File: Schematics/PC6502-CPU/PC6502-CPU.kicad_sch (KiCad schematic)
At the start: 71 parts, among them J1 BUS, J2 CONSOLE, J4 TEST, J5 Conn_02x05_Odd_Even, J6 Conn_02x02_Odd_Even, U1 MC68B50, U2 628128_DIP32_SSOP32, U3 SST39SF010, U4 ATF1502AS, U5 W65C02, U6 74AHC244, U7 74LS161, X1 CXO_DIP8, X2 ASCO

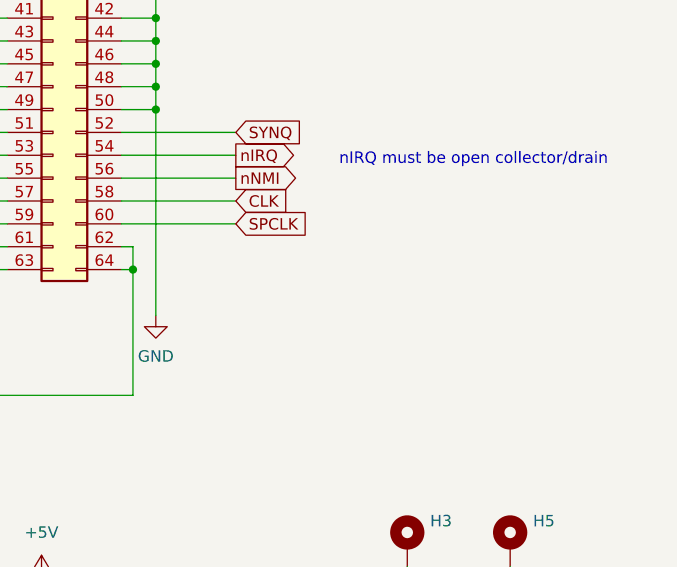
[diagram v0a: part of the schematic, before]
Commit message: Add Power/Storage PCB
Also tidied template
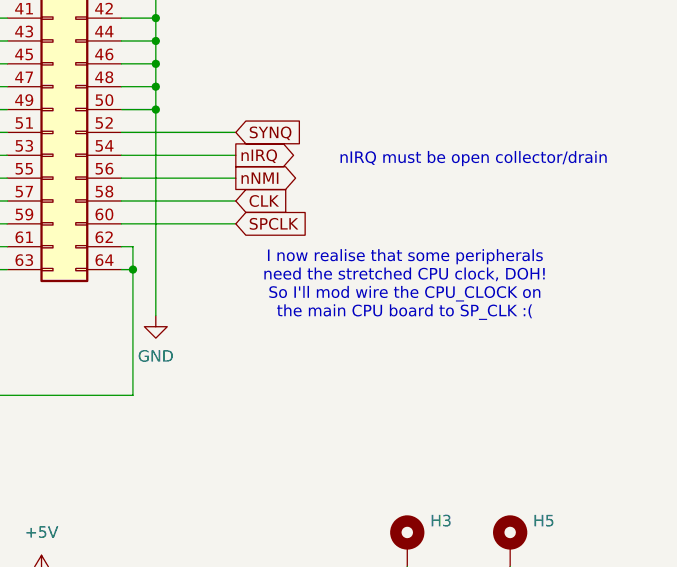
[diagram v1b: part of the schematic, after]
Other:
- note added: "I now realise that some peripherals need the stretched CPU clock, DOH! So I'll mod wire the CPU_CLOCK on the main CPU board to SP_CLK :("
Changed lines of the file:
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@@
+		)
+	)
+	(text "I now realise that some peripherals \nneed the stretched CPU clock, DOH!\nSo I'll mod wire the CPU_CLOCK on \nthe main CPU board to SP_CLK :("
+		(exclude_from_sim no)
+		(at 385.826 194.818 0)
+		(effects
+			(font
+				(size 1.27 1.27)
+			)
 		)
 	)

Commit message: Created V1.1 Schematic and PCB
A LOT of changes from v1.00;
removed clock stretcher (will now live in the CPLD)
moved the USB interface direct to the PCB
changed power pins
Added extra capacitance
Used Grant Searle's OSI basic and memory map to bring up the board
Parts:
- removed C10, C7: 100nF, Capacitor_SMD:C_0805_2012Metric, symbol Device:C
- removed D9: 1N4148, Diode_THT:D_DO-35_SOD27_P7.62mm_Horizontal, symbol Diode:1N4148
- removed J2: CONSOLE, Connector_PinHeader_2.54mm:PinHeader_1x03_P2.54mm_Horizontal, symbol Connector_Generic:Conn_01x03
- removed R17, R18: 0R, Resistor_SMD:R_0603_1608Metric_Pad0.98x0.95mm_HandSolder, symbol Device:R
- removed TP2, TP3, TP4: TestPoint, TestPoint:TestPoint_Loop_D1.80mm_Drill1.0mm_Beaded, symbol Connector:TestPoint
- removed U1: MC68B50, Package_DIP:DIP-24_W15.24mm_Socket, symbol Interface_UART:MC68B50
- removed U2: 628128_DIP32_SSOP32, Package_DIP:DIP-32_W15.24mm_LongPads, symbol Memory_RAM:628128_DIP32_SSOP32
- removed U7: 74LS161, Package_DIP:DIP-16_W7.62mm_Socket, symbol 74xx:74LS161
- removed X2: ASCO, Oscillator:Oscillator_SMD_EuroQuartz_XO91-4Pin_7.0x5.0mm_HandSoldering, symbol Oscillator:ASCO
- added C7: 47uF, Capacitor_SMD:C_1206_3216Metric, symbol Device:C_Polarized_US
- added U2: AS6C4008-55PCN, Package_DIP:DIP-32_W15.24mm, symbol Memory_RAM:AS6C4008-55PCN
- added U8: MCP130-450DI/TO, Package_TO_SOT_THT:TO-92_Inline, symbol Power_Supervisor:MCP130-xxxDxTO
- R15, R23, R24: value 4K7 -> 10K
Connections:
- net PHI2x2 is gone; now on net SYSCLK: X1.5 (OUT)
- net SPCLK is gone; now on net CPU_CLK: J1.60 (Pin_60)
- net +5V: now also C11.2, J1.12 (Pin_12), J1.16 (Pin_16), J1.20 (Pin_20), J1.24 (Pin_24), J1.28 (Pin_28), J1.32 (Pin_32), J1.36 (Pin_36), J1.4 (Pin_4), J1.40 (Pin_40), J1.44 (Pin_44), J1.48 (Pin_48), J1.8 (Pin_8), R6.2, R7.2, C7.1, U2.32 (VCC), U8.2 (VDD); no longer J1.59 (Pin_59), J1.61 (Pin_61), J1.62 (Pin_62), J1.63 (Pin_63), J1.64 (Pin_64), R15.1, R24.1
- net A0: now also U2.12 (A0)
- net A1: now also U2.11 (A1); no longer U4.11 (I/O/PD1)
- net A10: now also U2.23 (A10)
- net A11: now also U2.25 (A11)
- net A12: now also U2.4 (A12)
- net A13: now also U2.28 (A13)
- net A14: now also U2.3 (A14); no longer U3.29 (A14)
- net A2: now also U2.10 (A2); no longer U4.6 (I/O)
- net A3: now also U2.9 (A3); no longer U4.8 (I/O)
- net A4: now also U2.8 (A4)
- net A5: now also U2.7 (A5)
- net A6: now also U2.6 (A6)
- net A7: now also U2.5 (A7)
- net A8: now also U2.27 (A8)
- net A9: now also U2.26 (A9)
- net D0: now also U2.13 (DQ0)
- net D1: now also U2.14 (DQ1)
- net D2: now also U2.15 (DQ2)
- net D3: now also U2.17 (DQ3)
- net D4: now also U2.18 (DQ4)
- net D5: now also U2.19 (DQ5)
- net D6: now also U2.20 (DQ6)
- net D7: now also U2.21 (DQ7)
- net GND: now also C11.1, J1.64 (Pin_64), R15.2, R24.2, C7.2, U2.16 (VSS), U8.3 (VSS); no longer C11.2, J1.12 (Pin_12), J1.16 (Pin_16), J1.20 (Pin_20), J1.24 (Pin_24), J1.28 (Pin_28), J1.32 (Pin_32), J1.36 (Pin_36), J1.4 (Pin_4), J1.40 (Pin_40), J1.44 (Pin_44), J1.48 (Pin_48), J1.8 (Pin_8), R6.2, R7.2
- net RAM_A15: now also U2.31 (A15); no longer J4.2 (Pin_2), U6.13 (2A2)
- net RAM_A16: now also U2.2 (A16); no longer U6.11 (2A3)
- net nBUSRQ: now also J1.61 (Pin_61); no longer J1.55 (Pin_55)
- net nIRQ: now also U6.11 (2A3)
- net nR: now also U2.24 (OE#)
- net nRAM_CS: now also U2.22 (CE#)
- net nRES: now also J1.63 (Pin_63), J4.6 (Pin_6), RN1.4 (R3), U4.8 (I/O), U6.6 (1A2), U8.1 (~{RST}); no longer C11.1, J1.57 (Pin_57), R15.2
- net nW: now also U2.29 (WE#)
- net RDY: now reaches R19.2, U5.2 (RDY)
- net RDY: now also J1.57 (Pin_57)
- net at R23.2: now also U2.30 (A17)
- net nVP: now reaches U5.1 (VPB)
- net nVP: now also J1.59 (Pin_59)
- net at D8.1 (K): now also U6.9 (2Y3); no longer R7.1
- net at D8.2 (A): now also R7.1; no longer U6.9 (2Y3)
- net nRXF: now reaches U4.1 (I/GCLR)
- net nWR_FT: now reaches U4.41 (I/O/GCLK3)
- net nTXE: now reaches U4.44 (I/OE1)
- net at R6.1: now also D7.2 (A); no longer D7.1 (K)
- net at U6.7 (2Y2): now also D7.1 (K); no longer D7.2 (A)
- net 6850_E renamed nRD_FT
- net CLK renamed SYSCLK
- net ROM_A16 renamed ROM_A14
- net ROM_A14: now also U3.29 (A14); no longer U3.2 (A16)
- removed net nCONSOLE_CS: J4.6 (Pin_6), RN1.4 (R3), U4.29 (I/O), U6.6 (1A2)
- net nSLOW renamed nSLOW0
- net nSLOW0: now also U4.11 (I/O/PD1)
- new net: R15.1, U3.2 (A16)
- new net: R24.1, U2.1 (A18)
- new net RAM_A17: U4.29 (I/O)
- new net nSLOW1: J1.55 (Pin_55), J4.2 (Pin_2), U4.6 (I/O), U6.13 (2A2)
- no-connect marks 13 -> 8
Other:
- added sheet 60FAKE50 (60FAKE50.kicad_sch)
- note added: "CPU_CLK is the stretched version of CLK. Use nSLOW0 and nSLOW1 to slow the clock down"
- note added: "FLAGs are passed to the CPLD The CPLD "pretends" to be the 6850 register for status"
- note added: "For AS6C1008 remove R24"
- note added: "IRQ"
- note added: "MCP130 has internal 5K1 Pull up on ~{RST}"
- note added: "RESET"
- note added: "SLOW0"
- note added: "SLOW1"
- note removed: "CONSOLE"
- note removed: "I now realise that some peripherals need the stretched CPU clock, DOH! So I'll mod wire the CPU_CLOCK on the main CPU board to SP_CLK :("
- note removed: "If ROM isn't working, take OE to RnW direct"
- note removed: "RAMA15"
- note removed: "RAMA16"
- note removed: "SLOW"
- moved on the sheet: D7, D8, J5, R10, R13, R14, R16, S1

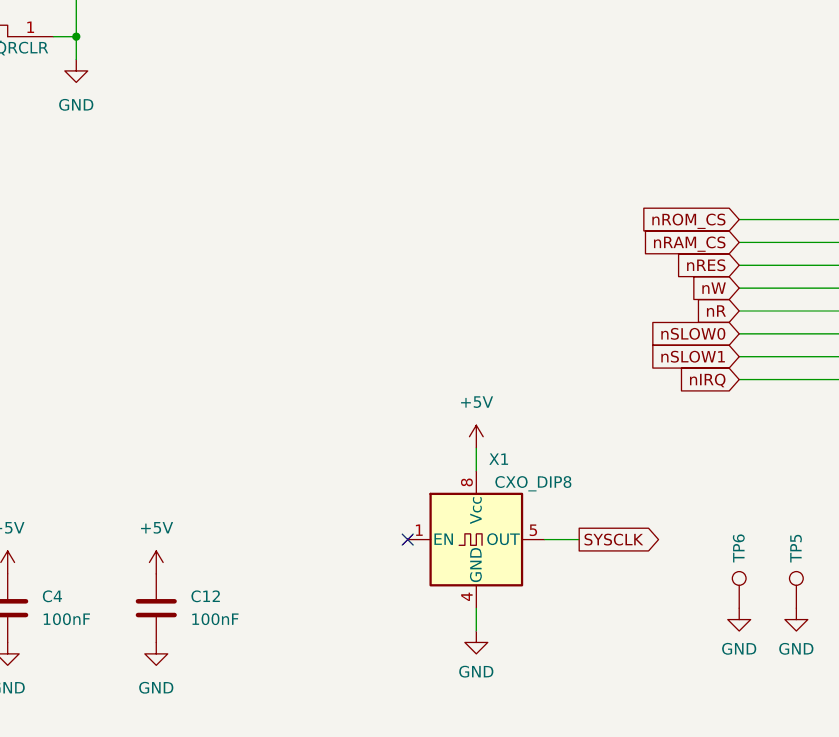
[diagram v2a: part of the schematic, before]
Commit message: FT245 WRITE signal correction
I had it marked as active low when it's active high, updated.
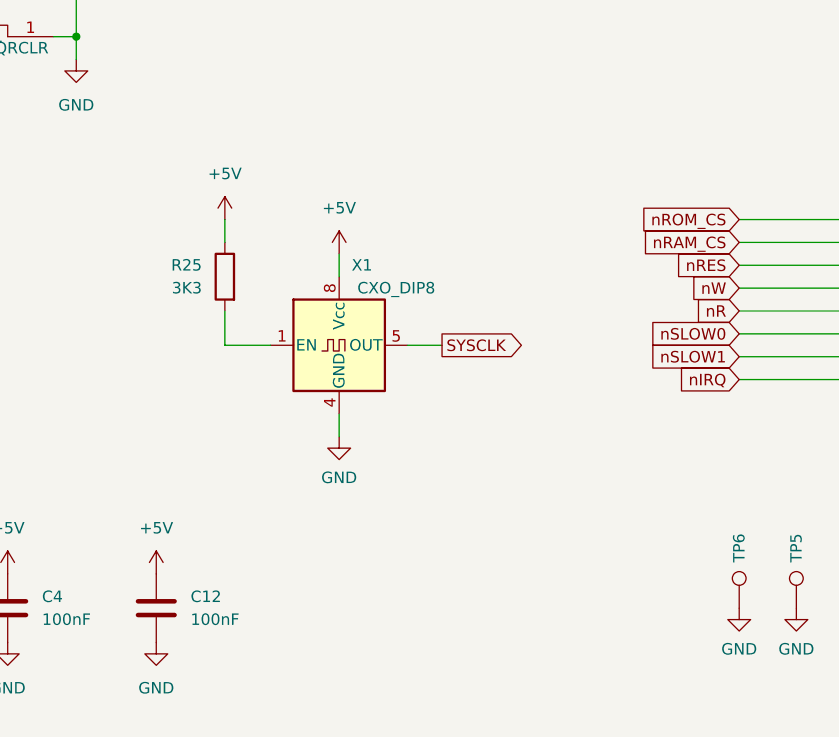
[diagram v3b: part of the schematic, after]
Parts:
- added R25: 3K3, Resistor_SMD:R_0603_1608Metric_Pad0.98x0.95mm_HandSolder, symbol Device:R
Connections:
- net +5V: now also R25.1
- net at X1.1 (EN): now also R25.2
- no-connect marks 8 -> 7
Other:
- moved on the sheet: X1
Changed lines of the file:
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@@
 	)
 	(no_connect
-		(at 124.46 257.81)
-	)
-	(no_connect
 		(at 64.77 149.86)
 	)
@@
 	(wire
 		(pts
+			(xy 104.14 236.22) (xy 104.14 232.41)
+		)
+		(stroke
+			(width 0)
+			(type default)
+		)
+	)
+	(wire
+		(pts
 			(xy 161.29 82.55) (xy 161.29 90.17)
 		)
@@
 	(wire
 		(pts
-			(xy 139.7 257.81) (xy 143.51 257.81)
+			(xy 124.46 236.22) (xy 128.27 236.22)
 		)
 		(stroke
@@
 	(wire
 		(pts
-			(xy 132.08 247.65) (xy 132.08 250.19)
+			(xy 116.84 226.06) (xy 116.84 228.6)
 		)
 		(stroke
@@
 		)
 	)
+	(wire
+		(pts
+			(xy 109.22 236.22) (xy 104.14 236.22)
+		)
+		(stroke
+			(width 0)
+			(type default)
+		)
+	)
 	(bus
 		(pts
@@
 	(wire
 		(pts
-			(xy 132.08 265.43) (xy 132.08 267.97)
+			(xy 116.84 243.84) (xy 116.84 246.38)
 		)
 		(stroke
@@
 	(wire
 		(pts
+			(xy 104.14 222.25) (xy 104.14 224.79)
+		)
+		(stroke
+			(width 0)
+			(type default)
+		)
+	)
+	(wire
+		(pts
 			(xy 86.36 43.18) (xy 71.12 43.18)
 		)
@@
 	(global_label "SYSCLK"
 		(shape output)
-		(at 143.51 257.81 0)
+		(at 128.27 236.22 0)
 		(fields_autoplaced yes)
 		(effects
@@
 		)
 		(property "Intersheetrefs" "${INTERSHEET_REFS}"
-			(at 153.5709 257.81 0)
+			(at 138.3309 236.22 0)
 			(effects
 				(font
@@
 	(symbol
 		(lib_id "power:+5V")
-		(at 132.08 247.65 0)
+		(at 116.84 226.06 0)
 		(unit 1)
 		(exclude_from_sim no)
@@
 		(fields_autoplaced yes)
 		(property "Reference" "#PWR033"
-			(at 132.08 251.46 0)
+			(at 116.84 229.87 0)
 			(effects
 				(font
@@
 		)
 		(property "Value" "+5V"
-			(at 132.08 242.57 0)
+			(at 116.84 220.98 0)
 			(effects
 				(font
@@
 		)
 		(property "Footprint" ""
-			(at 132.08 247.65 0)
+			(at 116.84 226.06 0)
 			(effects
 				(font
@@
 		)
 		(property "Datasheet" ""
-			(at 132.08 247.65 0)
+			(at 116.84 226.06 0)
 			(effects
 				(font
@@
 		)
 		(property "Description" ""
-			(at 132.08 247.65 0)
+			(at 116.84 226.06 0)
 			(effects
 				(font
@@
 	(symbol
 		(lib_id "power:GND")
-		(at 132.08 267.97 0)
+		(at 116.84 246.38 0)
 		(unit 1)
 		(exclude_from_sim no)
@@
 		(fields_autoplaced yes)
 		(property "Reference" "#PWR07"
-			(at 132.08 274.32 0)
+			(at 116.84 252.73 0)
 			(effects
 				(font
@@
 		)
 		(property "Value" "GND"
-			(at 132.08 272.5325 0)
+			(at 116.84 250.9425 0)
 			(effects
 				(font
@@
 		)
 		(property "Footprint" ""
-			(at 132.08 267.97 0)
+			(at 116.84 246.38 0)
 			(effects
 				(font
@@
 		)
 		(property "Datasheet" ""
-			(at 132.08 267.97 0)
+			(at 116.84 246.38 0)
 			(effects
 				(font
@@
 		)
 		(property "Description" ""
-			(at 132.08 267.97 0)
+			(at 116.84 246.38 0)
 			(effects
 				(font
@@
 	)
 	(symbol
+		(lib_id "Device:R")
+		(at 104.14 228.6 0)
+		(mirror y)
+		(unit 1)
+		(exclude_from_sim no)
+		(in_bom yes)
+		(on_board yes)
+		(dnp no)
+		(fields_autoplaced yes)
+		(property "Reference" "R25"
+			(at 101.6 227.3299 0)
+			(effects
+				(font
+					(size 1.27 1.27)
+				)
+				(justify left)
+			)
+		)
+		(property "Value" "3K3"
+			(at 101.6 229.8699 0)
+			(effects
+				(font
+					(size 1.27 1.27)
+				)
+				(justify left)
+			)
+		)
+		(property "Footprint" "Resistor_SMD:R_0603_1608Metric_Pad0.98x0.95mm_HandSolder"
+			(at 105.918 228.6 90)
+			(effects
+				(font
+					(size 1.27 1.27)
+				)
+				(hide yes)
+			)
+		)
+		(property "Datasheet" "~"
+			(at 104.14 228.6 0)
+			(effects
+				(font
+					(size 1.27 1.27)
+				)
+				(hide yes)
+			)
+		)
+		(property "Description" ""
+			(at 104.14 228.6 0)
+			(effects
+				(font
+					(size 1.27 1.27)
+				)
+			)
+		)
+		(pin "1"
+		)
+		(pin "2"
+		)
+		(instances
+			(project "PC6502-CPU"
+				(path "/f3365b77-bdc1-4fa0-8030-841dab6ab2be"
+					(reference "R25")
+					(unit 1)
+				)
+			)
+		)
+	)
+	(symbol
 		(lib_id "power:+5V")
 		(at 134.62 66.04 0)
@@
 	)
 	(symbol
+		(lib_id "power:+5V")
+		(at 104.14 222.25 0)
+		(mirror y)
+		(unit 1)
+		(exclude_from_sim no)
+		(in_bom yes)
+		(on_board yes)
+		(dnp no)
+		(fields_autoplaced yes)
+		(property "Reference" "#PWR050"
+			(at 104.14 226.06 0)
+			(effects
+				(font
+					(size 1.27 1.27)
+				)
+				(hide yes)
+			)
+		)
+		(property "Value" "+5V"
+			(at 104.14 217.17 0)
+			(effects
+				(font
+					(size 1.27 1.27)
+				)
+			)
+		)
+		(property "Footprint" ""
+			(at 104.14 222.25 0)
+			(effects
+				(font
+					(size 1.27 1.27)
+				)
+				(hide yes)
+			)
+		)
+		(property "Datasheet" ""
+			(at 104.14 222.25 0)
+			(effects
+				(font
+					(size 1.27 1.27)
+				)
+				(hide yes)
+			)
+		)
+		(property "Description" ""
+			(at 104.14 222.25 0)
+			(effects
+				(font
+					(size 1.27 1.27)
+				)
+			)
+		)
+		(pin "1"
+		)
+		(instances
+			(project "PC6502-CPU"
+				(path "/f3365b77-bdc1-4fa0-8030-841dab6ab2be"
+					(reference "#PWR050")
+					(unit 1)
+				)
+			)
+		)
+	)
+	(symbol
 		(lib_id "Device:LED")
 		(at 250.19 222.25 0)
@@
 	(symbol
 		(lib_id "Oscillator:CXO_DIP8")
-		(at 132.08 257.81 0)
+		(at 116.84 236.22 0)
 		(unit 1)
 		(exclude_from_sim no)
@@
 		(dnp no)
 		(property "Reference" "X1"
-			(at 134.62 248.92 0)
+			(at 119.38 227.33 0)
 			(effects
 				(font
@@
 		)
 		(property "Value" "CXO_DIP8"
-			(at 138.43 251.46 0)
+			(at 123.19 229.87 0)
 			(effects
 				(font
@@
 		)
 		(property "Footprint" "Oscillator:Oscillator_DIP-8"
-			(at 143.51 266.7 0)
+			(at 128.27 245.11 0)
 			(effects
 				(font
@@
 		)
 		(property "Datasheet" "http://cdn-reichelt.de/documents/datenblatt/B400/OSZI.pdf"
-			(at 129.54 257.81 0)
+			(at 114.3 236.22 0)
 			(effects
 				(font
@@
 		)
 		(property "Description" ""
-			(at 132.08 257.81 0)
+			(at 116.84 236.22 0)
 			(effects
 				(font

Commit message: FT245 label change
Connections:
- net nWR_FT renamed WR_FT
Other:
- sheet 60FAKE50 ports: added WR_FT; removed nWR_FT
- note added: "Note that the WRITE is active HIGH!"
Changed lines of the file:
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@@
 		)
 	)
+	(text "Note that the WRITE is active HIGH!"
+		(exclude_from_sim no)
+		(at 385.064 88.138 0)
+		(effects
+			(font
+				(size 1.27 1.27)
+			)
+		)
+	)
 	(text "SLOW0\n"
 		(exclude_from_sim no)
@@
 		)
 	)
-	(global_label "nWR_FT"
+	(global_label "WR_FT"
 		(shape input)
 		(at 370.84 63.5 180)
@@
 		)
 		(property "Intersheetrefs" "${INTERSHEET_REFS}"
-			(at 360.9606 63.5 0)
+			(at 362.1096 63.5 0)
 			(effects
 				(font
@@
 		)
 	)
-	(global_label "nWR_FT"
+	(global_label "WR_FT"
 		(shape output)
 		(at 190.5 144.78 0)
@@
 		)
 		(property "Intersheetrefs" "${INTERSHEET_REFS}"
-			(at 200.3794 144.78 0)
+			(at 199.2304 144.78 0)
 			(effects
 				(font
@@
 			)
 		)
-		(pin "nWR_FT" input
+		(pin "WR_FT" input
 			(at 379.73 63.5 180)
 			(effects

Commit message: V1.1 CPU, VIA and POWER PCBs uploaded
A simpler CPU board (direct link to FT245R, 74161 removed and some tidying of tracks). Fixed a couple of floating inputs to RAM/ROM
VIA is much simpler, having just the one VIA chip.
POWER board has USB-PD and a 24VDC input for higher power stuff in the future.
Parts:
- C1, C11, C12, C2, C3, C4, C5, C8, C9: LCSC (none) -> C49678
- D1, D2, D3, D4, D5, D6, D7, D8, J4, J5, RN1, S1, TP5, TP6, U2, U3, U4, U5, U6, U8, X1: LCSC (none) -> DNF; now not fitted
- FOX1: now left out of the parts list
- H3, H4, H5, H6: now not fitted; now left out of the parts list
- J1: now not fitted
- J6: LCSC (none) -> D NF; now not fitted
- R1, R11, R16, R2, R3, R4, R5, R6, R7: LCSC (none) -> C23179
- R10, R12, R13, R14, R15, R23, R24: LCSC (none) -> C25744
- R19, R20, R22, R25, R8, R9: LCSC (none) -> C25890
- R21: LCSC (none) -> DNF
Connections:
- net RAM_A17 is gone; now on net WR_FT: U4.29 (I/O)
- net WR_FT: no longer U4.41 (I/O/GCLK3)
- net nR: no longer U3.24 (OE)
- new net ROM_nR: U3.24 (OE), U4.41 (I/O/GCLK3)
- no-connect marks 7 -> 8
